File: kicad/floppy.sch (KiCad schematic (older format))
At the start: 24 parts, among them J4 Conn_02x17_Odd_Even, U13 74HC04, U15 74LS06, U17 WD1770, U18 74LS06, U19 74LS08, Y1 8Mhz

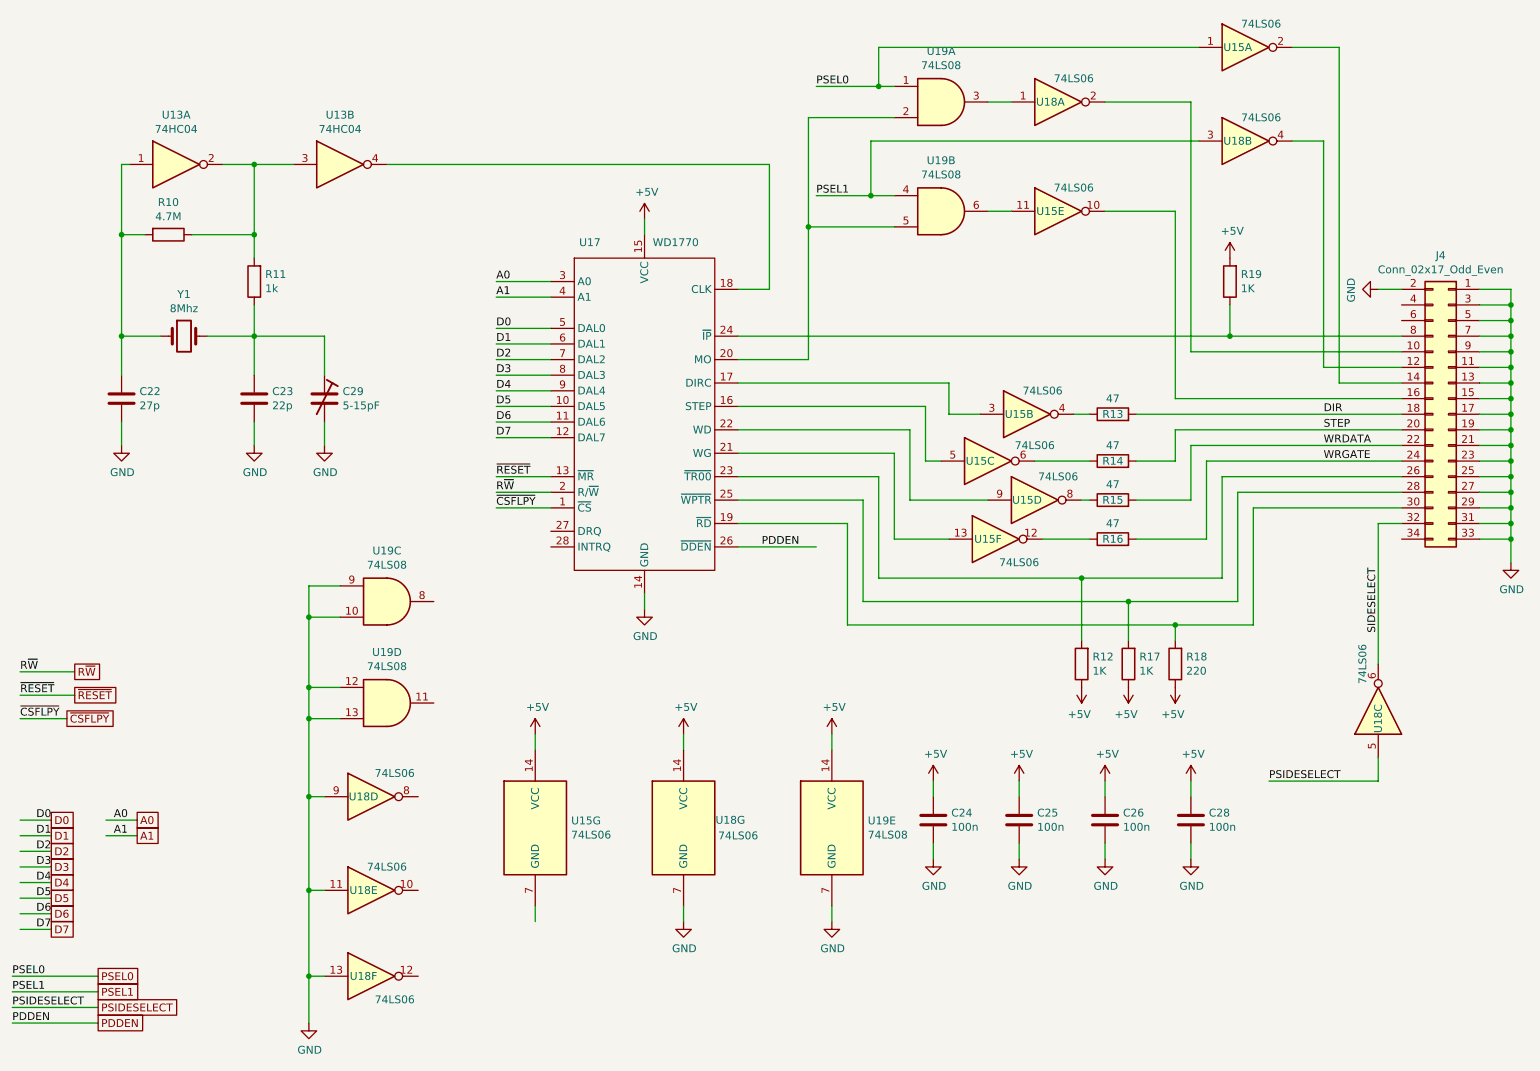
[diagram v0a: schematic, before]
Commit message: Adding PCB layout
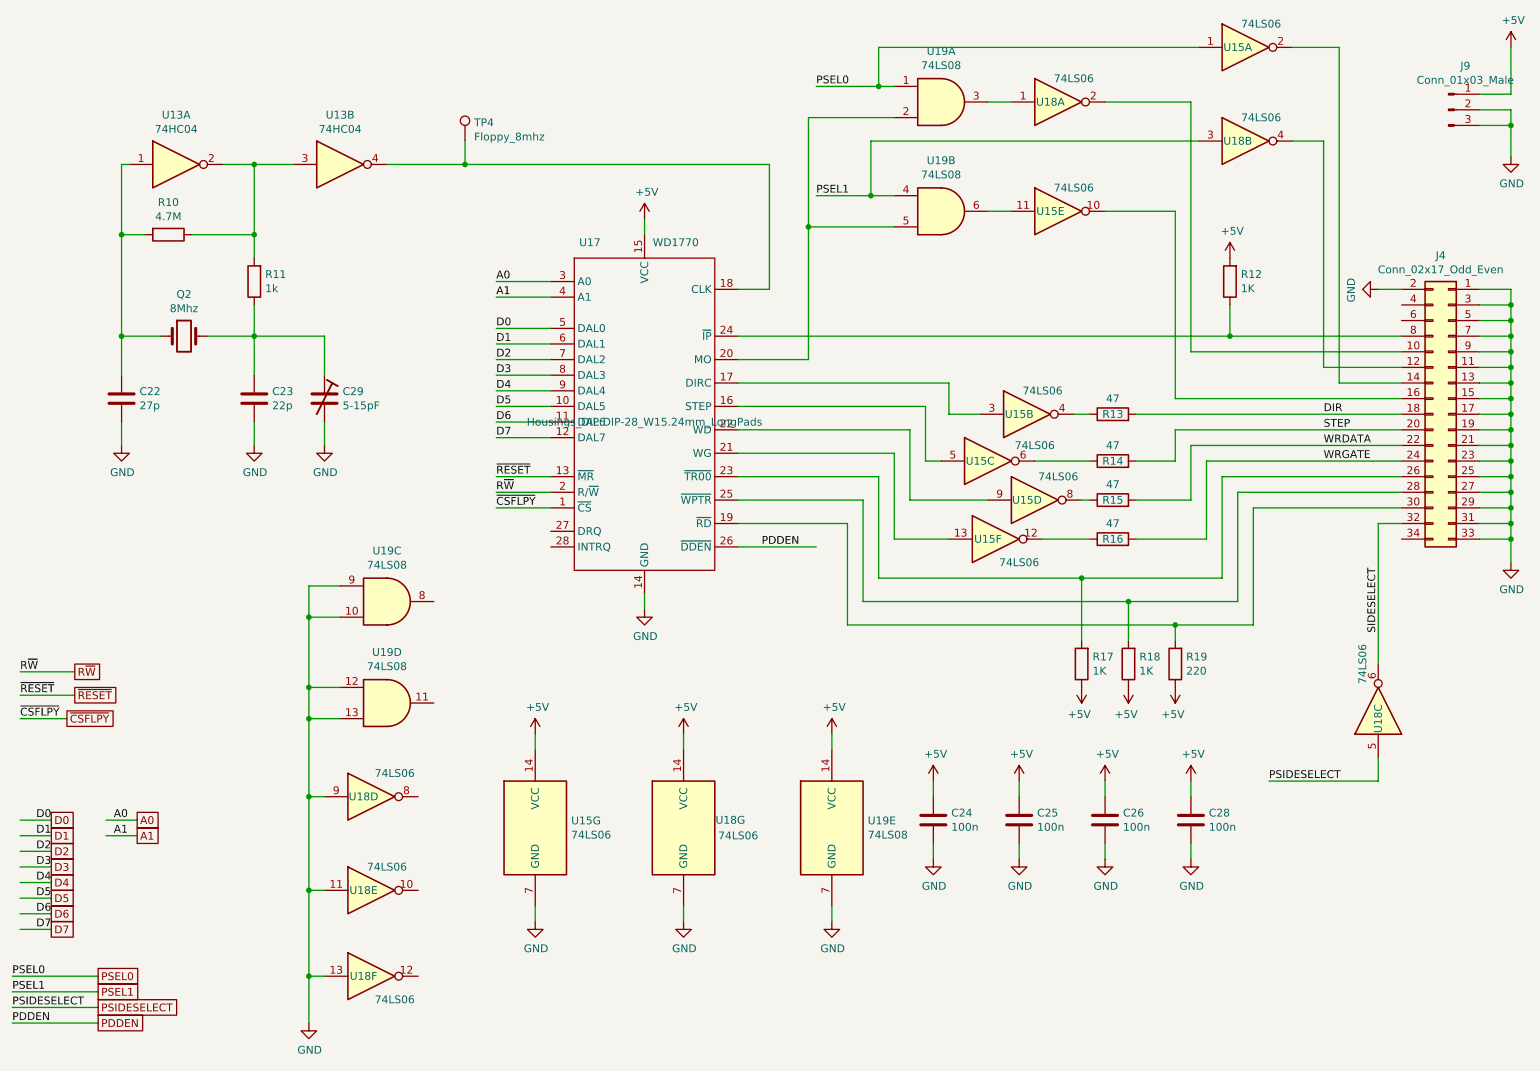
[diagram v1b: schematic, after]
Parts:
- added J9: Conn_01x03_Male, Connectors_Molex:Molex_KK-6410-03_03x2.54mm_Straight, symbol Connector:Conn_01x03_Male
- added TP4: Floppy_8mhz, Connectors:Pin_d1.0mm_L10.0mm, symbol Connector:TestPoint
- C29: footprint (none) -> mylib:C-TRIMMER-5
- J4: footprint (none) -> Connectors_Multicomp:Multicomp_MC9A12-3434_2x17x2.54mm_Straight
- Q2: renamed from Y1; footprint (none) -> Crystals:Crystal_HC18-U_Vertical
- R12: renamed from R19; footprint Resistors_THT:R_Axial_DIN0207_L6.3mm_D2.5mm_P7.62mm_Horizontal -> Resistors_THT:R_Axial_DIN0204_L3.6mm_D1.6mm_P7.62mm_Horizontal
- R13, R14, R15, R16: footprint Resistors_THT:R_Axial_DIN0207_L6.3mm_D2.5mm_P7.62mm_Horizontal -> Resistors_THT:R_Axial_DIN0204_L3.6mm_D1.6mm_P7.62mm_Horizontal
- R17: renamed from R12; footprint Resistors_THT:R_Axial_DIN0207_L6.3mm_D2.5mm_P7.62mm_Horizontal -> Resistors_THT:R_Axial_DIN0204_L3.6mm_D1.6mm_P7.62mm_Horizontal
- R18: renamed from R17; footprint Resistors_THT:R_Axial_DIN0207_L6.3mm_D2.5mm_P7.62mm_Horizontal -> Resistors_THT:R_Axial_DIN0204_L3.6mm_D1.6mm_P7.62mm_Horizontal
- R19: renamed from R18; footprint Resistors_THT:R_Axial_DIN0207_L6.3mm_D2.5mm_P7.62mm_Horizontal -> Resistors_THT:R_Axial_DIN0204_L3.6mm_D1.6mm_P7.62mm_Horizontal
- U13, U15, U18, U19: footprint (none) -> Housings_DIP:DIP-14_W7.62mm_LongPads
- U17: footprint (none) -> Housings_DIP:DIP-28_W15.24mm_LongPads
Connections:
- wire segments 199 -> 207

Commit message: Adding PCB
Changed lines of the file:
@@
 F 0 "U17" H 4600 4450 50  0000 C CNN
 F 1 "WD1770" H 5150 4450 50  0000 C CNN
-F 2 "Housings_DIP:DIP-28_W15.24mm_LongPads" H 4950 3300 50  0000 C CNN
+F 2 "Housings_DIP:DIP-28_W15.24mm_LongPads" H 4950 3300 50  0001 C CNN
 F 3 "" H 4950 3300 50  0001 C CNN
 	1    4950 3300
